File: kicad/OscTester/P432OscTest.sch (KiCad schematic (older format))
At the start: 12 parts, among them J1 Power-XP6, J2 Freq-XP1, J3 Filter-XP7, J4 Volume-XP6, J5 Control-XP5, SW1 SW_DIP_x04

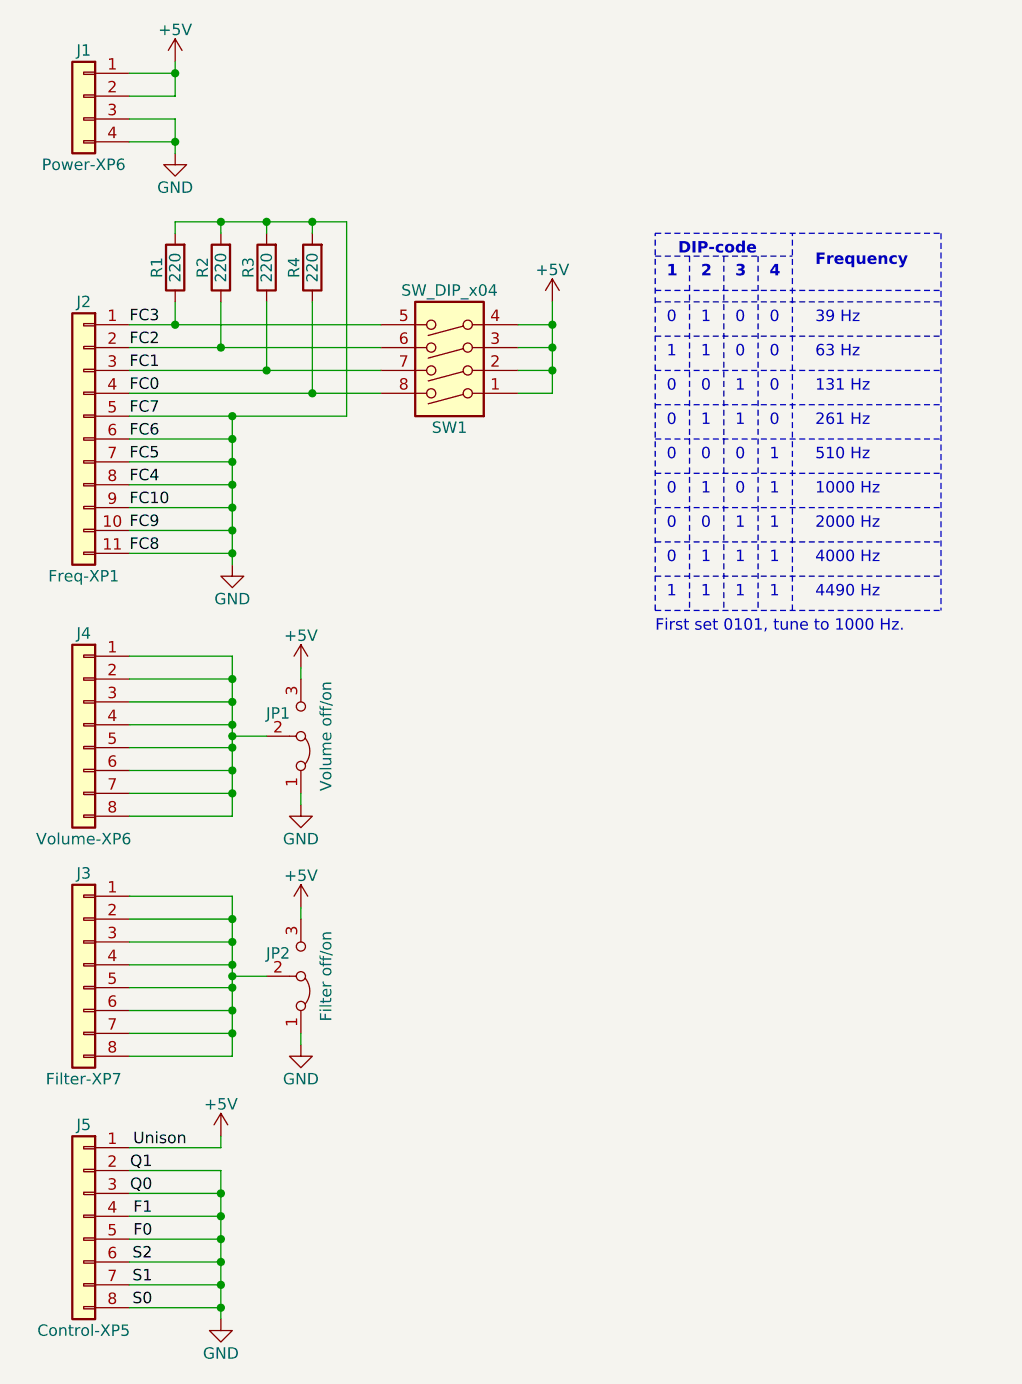
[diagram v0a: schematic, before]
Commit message: Unison bit set to 0 to test all 8 voices
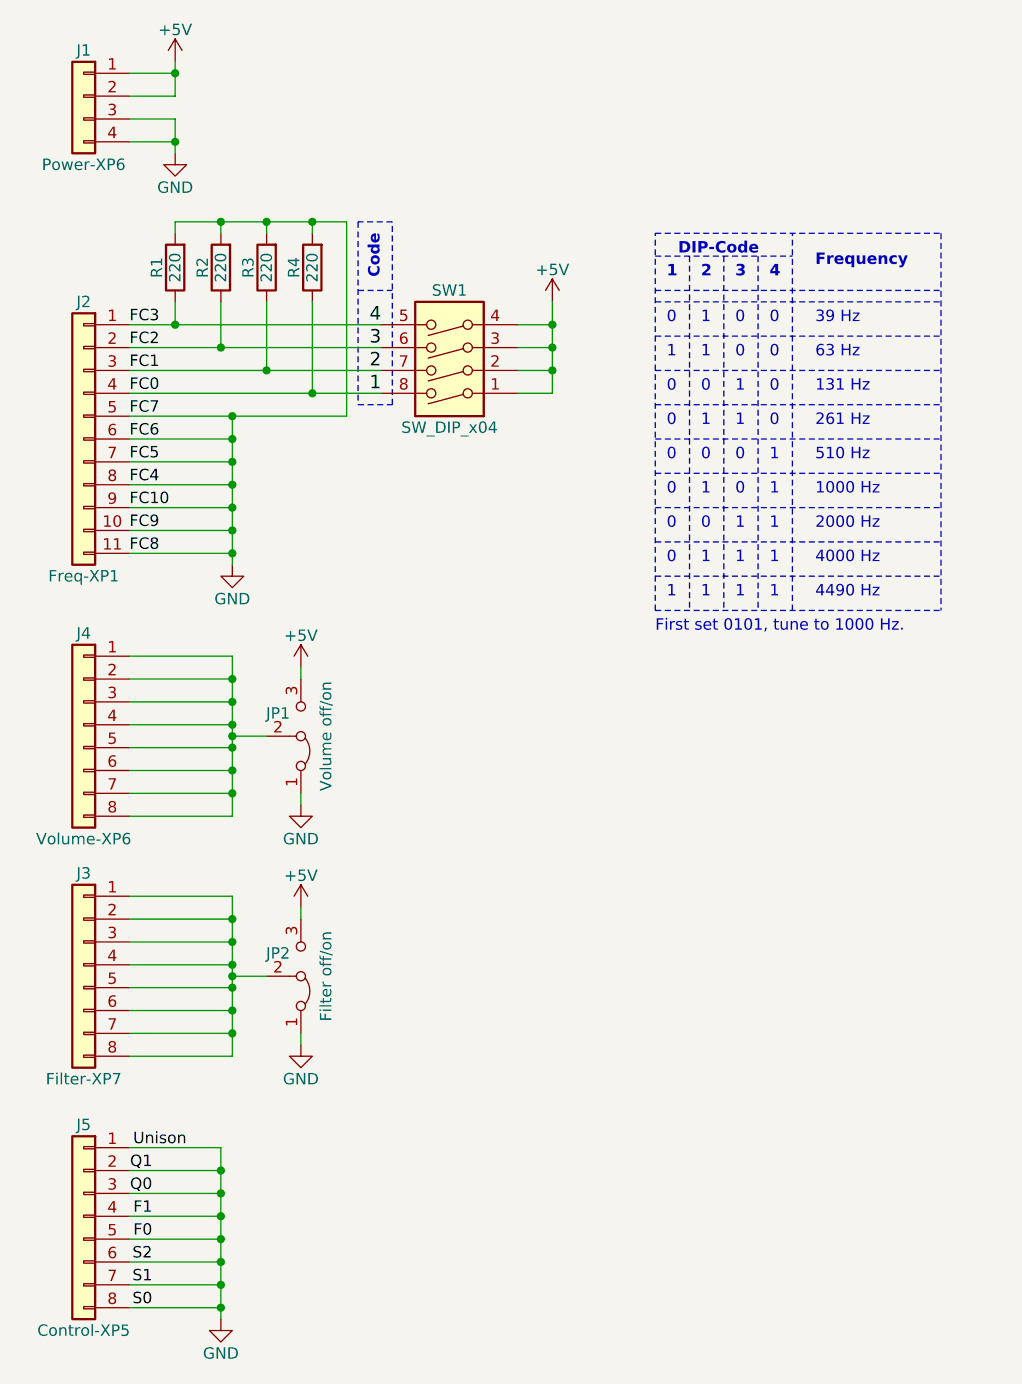
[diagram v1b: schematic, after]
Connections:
- net +5V: no longer J5.1 (Pin_1)
- net GND: now also J5.1 (Pin_1)
- net FC0 renamed 1
- net FC1 renamed 2
- net FC2 renamed 3
- net FC3 renamed 4
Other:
- note added: "Code"
- note added: "DIP-Code"
- note removed: "DIP-code"
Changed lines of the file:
@@
 	-1   0    0    -1
 $EndComp
-Text Label 1450 5600 2    50   ~ 0
-Unison
 Text Label 1300 5700 2    50   ~ 0
 Q1
@@
 	1600 1600 1600 1550
 Wire Wire Line
-	2150 1550 2150 2400
-Wire Wire Line
-	2150 2400 1650 2400
-Connection ~ 1650 2400
-Wire Wire Line
 	1200 4500 1650 4500
 Wire Wire Line
@@
 Wire Wire Line
 	1650 3800 1650 3850
-$Comp
-L power:+5V #PWR03
-U 1 1 5E9BDAFE
-P 3050 1900
-F 0 "#PWR03" H 3050 1750 50  0001 C CNN
-F 1 "+5V" H 3050 2040 50  0000 C CNN
-F 2 "" H 3050 1900 50  0001 C CNN
-F 3 "" H 3050 1900 50  0001 C CNN
-	1    3050 1900
-	1    0    0    -1
-$EndComp
-Wire Wire Line
-	2900 2000 3050 2000
-Wire Wire Line
-	3050 2000 3050 1900
-Wire Wire Line
-	2900 2100 3050 2100
-Wire Wire Line
-	3050 2100 3050 2000
-Connection ~ 3050 2000
-Wire Wire Line
-	3050 2200 3050 2100
-Connection ~ 3050 2100
-Wire Wire Line
-	2900 2200 3050 2200
-Wire Wire Line
-	2900 2300 3050 2300
-Wire Wire Line
-	3050 2300 3050 2200
-Connection ~ 3050 2200
 Wire Notes Line
 	3500 1700 4100 1700
@@
 Text Notes 4000 1800 0    50   ~ 10
 4
-$Comp
-L power:+5V #PWR09
-U 1 1 5EA0120D
-P 1600 5550
-F 0 "#PWR09" H 1600 5400 50  0001 C CNN
-F 1 "+5V" H 1600 5690 50  0000 C CNN
-F 2 "" H 1600 5550 50  0001 C CNN
-F 3 "" H 1600 5550 50  0001 C CNN
-	1    1600 5550
-	1    0    0    -1
-$EndComp
-Wire Wire Line
-	1600 5600 1600 5550
 Wire Notes Line
 	3500 1850 4750 1850
@@
 Wire Wire Line
 	1800 1550 2000 1550
-Connection ~ 2000 1550
-Wire Wire Line
-	2000 1550 2150 1550
 Wire Wire Line
 	1200 1100 1400 1100
@@
 	-1   0    0    -1
 $EndComp
-$Comp
-L Switch:SW_DIP_x04 SW1
-U 1 1 5E857AA0
-P 2600 2100
-F 0 "SW1" H 2600 2450 50  0000 C CNN
-F 1 "SW_DIP_x04" H 2600 1850 50  0000 C CNN
-F 2 "Button_Switch_THT:SW_DIP_SPSTx04_Slide_9.78x12.34mm_W7.62mm_P2.54mm" H 2600 2100 50  0001 C CNN
-F 3 "~" H 2600 2100 50  0001 C CNN
-	1    2600 2100
-	-1   0    0    1
-$EndComp
 Wire Wire Line
 	1400 1900 1400 2000
-Wire Wire Line
-	2000 2300 2300 2300
-Connection ~ 2000 2300
-Wire Wire Line
-	2300 2200 1800 2200
-Connection ~ 1800 2200
-Wire Wire Line
-	2300 2100 1600 2100
-Connection ~ 1600 2100
-Wire Wire Line
-	2300 2000 1400 2000
-Connection ~ 1400 2000
 $Comp
 L Jumper:Jumper_3_Bridged12 JP2
@@
 First set 0101, tune to 1000 Hz.
 Text Notes 3600 1700 0    50   ~ 10
-DIP-code
+DIP-Code
 Wire Notes Line
 	4100 3250 4100 1600
@@
 Wire Notes Line
 	3500 1600 4750 1600
+Wire Wire Line
+	1600 5600 1600 5700
+Connection ~ 1600 5700
+Connection ~ 1400 2000
+Connection ~ 1600 2100
+Connection ~ 1800 2200
+Connection ~ 2000 2300
+Connection ~ 2000 1550
+Connection ~ 1650 2400
+Text Notes 2300 1800 1    50   ~ 10
+Code
+Wire Notes Line
+	2200 1550 2200 2350
+Wire Notes Line
+	2200 1850 2350 1850
+Wire Notes Line
+	2350 1550 2200 1550
+Wire Notes Line
+	2350 2350 2350 1550
+Wire Notes Line
+	2200 2350 2350 2350
+Text Label 2250 2000 0    59   ~ 0
+4
+Text Label 2250 2100 0    59   ~ 0
+3
+Text Label 2250 2200 0    59   ~ 0
+2
+Text Label 2250 2300 0    59   ~ 0
+1
+Wire Wire Line
+	2300 2000 1400 2000
+Wire Wire Line
+	2300 2100 1600 2100
+Wire Wire Line
+	2300 2200 1800 2200
+Wire Wire Line
+	2000 2300 2300 2300
+Wire Wire Line
+	2000 1550 2150 1550
+Wire Wire Line
+	2150 2400 1650 2400
+Wire Wire Line
+	2150 1550 2150 2400
+Connection ~ 3050 2200
+Wire Wire Line
+	3050 2300 3050 2200
+Wire Wire Line
+	2900 2300 3050 2300
+Wire Wire Line
+	2900 2200 3050 2200
+Connection ~ 3050 2100
+Wire Wire Line
+	3050 2200 3050 2100
+Connection ~ 3050 2000
+Wire Wire Line
+	3050 2100 3050 2000
+Wire Wire Line
+	2900 2100 3050 2100
+Wire Wire Line
+	3050 2000 3050 1900
+Wire Wire Line
+	2900 2000 3050 2000
+$Comp
+L power:+5V #PWR03
+U 1 1 5E9BDAFE
+P 3050 1900
+F 0 "#PWR03" H 3050 1750 50  0001 C CNN
+F 1 "+5V" H 3050 2040 50  0000 C CNN
+F 2 "" H 3050 1900 50  0001 C CNN
+F 3 "" H 3050 1900 50  0001 C CNN
+	1    3050 1900
+	1    0    0    -1
+$EndComp
+$Comp
+L Switch:SW_DIP_x04 SW1
+U 1 1 5E857AA0
+P 2600 2100
+F 0 "SW1" H 2600 1850 50  0000 C CNN
+F 1 "SW_DIP_x04" H 2600 2450 50  0000 C CNN
+F 2 "Button_Switch_THT:SW_DIP_SPSTx04_Slide_9.78x12.34mm_W7.62mm_P2.54mm" H 2600 2100 50  0001 C CNN
+F 3 "~" H 2600 2100 50  0001 C CNN
+	1    2600 2100
+	-1   0    0    1
+$EndComp
+Text Label 1450 5600 2    50   ~ 0
+Unison
 $EndSCHEMATC

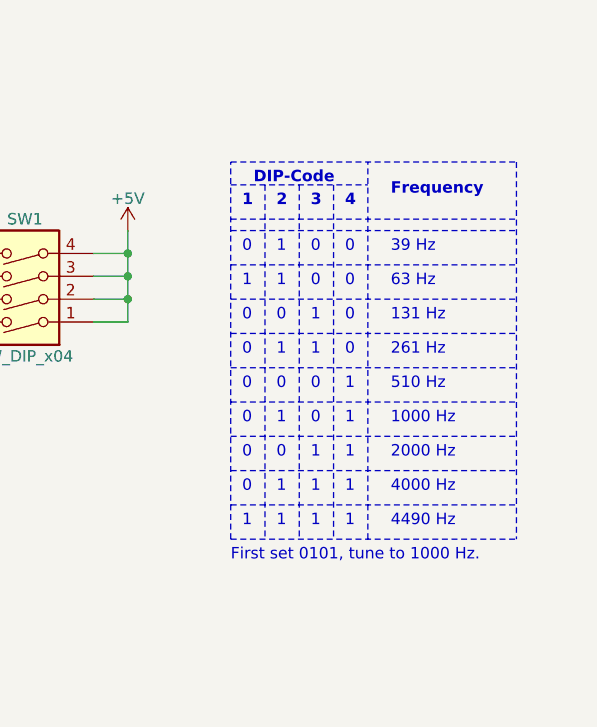
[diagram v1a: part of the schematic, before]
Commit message: Freq values changed to the correct ones.
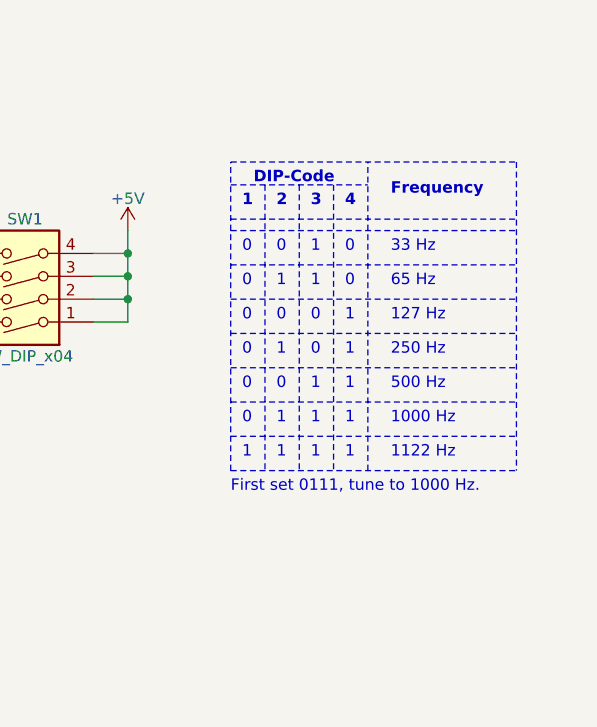
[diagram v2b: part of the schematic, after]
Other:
- note added: "1122 Hz"
- note added: "127 Hz"
- note added: "250 Hz"
- note added: "33 Hz"
- note added: "500 Hz"
- note added: "65 Hz"
- note added: "First set 0111, tune to 1000 Hz."
- note removed: "131 Hz"
- note removed: "2000 Hz"
- note removed: "261 Hz"
- note removed: "39 Hz"
- note removed: "4000 Hz"
- note removed: "4490 Hz"
- note removed: "510 Hz"
- note removed: "63 Hz"
- note removed: "First set 0101, tune to 1000 Hz."
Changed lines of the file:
@@
 Wire Notes Line
 	3500 1850 4750 1850
-Wire Notes Line
-	3500 3100 4750 3100
 Wire Wire Line
 	1400 1550 1600 1550
@@
 0
 Text Notes 3700 2000 0    50   ~ 0
-1
-Text Notes 3850 2000 0    50   ~ 0
 0
 Text Notes 4000 2000 0    50   ~ 0
 0
 Text Notes 4200 2000 0    50   ~ 0
-39 Hz
-Text Notes 3850 2150 0    50   ~ 0
+33 Hz
+Text Notes 3550 2150 0    50   ~ 0
 0
 Text Notes 3700 2150 0    50   ~ 0
 1
 Text Notes 4200 2150 0    50   ~ 0
-63 Hz
+65 Hz
 Wire Notes Line
 	3500 2200 4750 2200
@@
 	3500 2350 4750 2350
 Text Notes 4200 2300 0    50   ~ 0
-131 Hz
+127 Hz
 Text Notes 3550 2300 0    50   ~ 0
 0
-Text Notes 3850 2300 0    50   ~ 0
-1
-Text Notes 3550 2150 0    50   ~ 0
+Text Notes 4000 2300 0    50   ~ 0
+1
+Text Notes 3850 2150 0    50   ~ 0
 1
 Text Notes 4000 2150 0    50   ~ 0
@@
 	3500 2650 4750 2650
 Text Notes 4200 2450 0    50   ~ 0
-261 Hz
+250 Hz
 Text Notes 3700 2450 0    50   ~ 0
 1
 Text Notes 3550 2450 0    50   ~ 0
 0
+Text Notes 3850 2450 0    50   ~ 0
+0
 Text Notes 4000 2450 0    50   ~ 0
-0
-Text Notes 3850 2450 0    50   ~ 0
 1
 Wire Notes Line
 	3500 2800 4750 2800
-Wire Notes Line
-	3500 2950 4750 2950
 Text Notes 4200 2600 0    50   ~ 0
-510 Hz
+500 Hz
 Text Notes 3550 2600 0    50   ~ 0
 0
-Text Notes 3850 2600 0    50   ~ 0
-0
 Text Notes 4000 2600 0    50   ~ 0
 1
-Wire Notes Line
-	3500 3250 4750 3250
 Text Notes 4200 2750 0    50   ~ 0
 1000 Hz
@@
 Text Notes 3550 2750 0    50   ~ 0
 0
-Text Notes 3850 2750 0    50   ~ 0
-0
 Text Notes 4000 2750 0    50   ~ 0
 1
 Text Notes 4200 2900 0    50   ~ 0
-2000 Hz
+1122 Hz
 Text Notes 3850 2900 0    50   ~ 0
 1
-Text Notes 3550 2900 0    50   ~ 0
-0
-Text Notes 3700 2900 0    50   ~ 0
-0
 Text Notes 4000 2900 0    50   ~ 0
 1
-Text Notes 4200 3050 0    50   ~ 0
-4000 Hz
-Text Notes 3550 3050 0    50   ~ 0
-0
-Text Notes 4000 3050 0    50   ~ 0
-1
-Text Notes 4200 3200 0    50   ~ 0
-4490 Hz
-Text Notes 4000 3200 0    50   ~ 0
-1
 Text Notes 3700 2300 0    50   ~ 0
 0
-Text Notes 4000 2300 0    50   ~ 0
+Text Notes 3850 2300 0    50   ~ 0
 0
 Wire Notes Line
 	3500 1900 4750 1900
-Text Notes 3700 3200 0    50   ~ 0
-1
-Text Notes 3700 3050 0    50   ~ 0
-1
-Wire Notes Line
-	3650 1700 3650 3250
-Wire Notes Line
-	3950 1700 3950 3250
-Wire Notes Line
-	3800 1700 3800 3250
 Text Notes 3700 2600 0    50   ~ 0
 0
-Text Notes 3850 3050 0    50   ~ 0
-1
-Text Notes 3550 3200 0    50   ~ 0
-1
-Text Notes 3850 3200 0    50   ~ 0
-1
-Text Notes 3500 3350 0    50   ~ 0
-First set 0101, tune to 1000 Hz.
+Text Notes 3500 3050 0    50   ~ 0
+First set 0111, tune to 1000 Hz.
 Text Notes 3600 1700 0    50   ~ 10
 DIP-Code
-Wire Notes Line
-	4100 3250 4100 1600
-Wire Notes Line
-	4750 1600 4750 3250
-Wire Notes Line
-	3500 3250 3500 1600
 Wire Notes Line
 	3500 1600 4750 1600
@@
 Text Label 1450 5600 2    50   ~ 0
 Unison
+Text Notes 3850 2000 0    50   ~ 0
+1
+Text Notes 3850 2600 0    50   ~ 0
+1
+Text Notes 3850 2750 0    50   ~ 0
+1
+Text Notes 3700 2900 0    50   ~ 0
+1
+Text Notes 3550 2900 0    50   ~ 0
+1
+Wire Notes Line
+	3500 2950 3500 1600
+Wire Notes Line
+	4750 1600 4750 2950
+Wire Notes Line
+	3500 2950 4750 2950
+Wire Notes Line
+	3650 1700 3650 2950
+Wire Notes Line
+	3950 1700 3950 2950
+Wire Notes Line
+	3800 1700 3800 2950
+Wire Notes Line
+	4100 2950 4100 1600
 $EndSCHEMATC
